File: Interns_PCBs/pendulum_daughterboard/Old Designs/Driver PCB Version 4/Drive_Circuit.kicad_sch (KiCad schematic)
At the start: 13 parts, among them IC1 MAX9928FAUA+, J2 Coil, Q1 BC858W, Q2 BD911

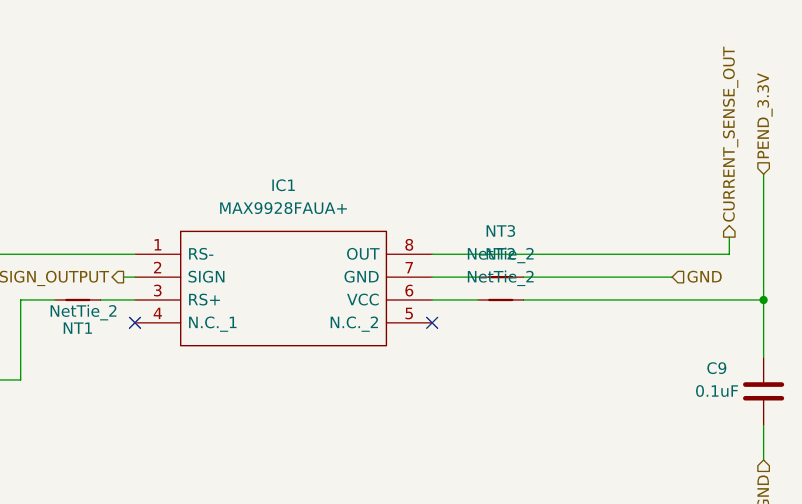
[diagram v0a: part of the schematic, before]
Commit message: Level Shifting Daughterboard
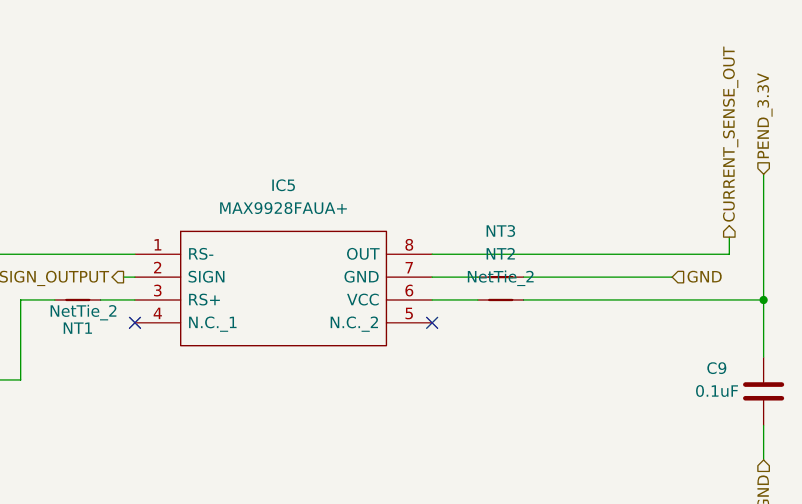
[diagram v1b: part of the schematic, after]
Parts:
- NT3: value NetTie_2 -> (none); footprint NetTie:NetTie-2_SMD_Pad0.5mm -> (none)
- renumbered IC1 to IC5
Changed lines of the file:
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@@
     (in_bom yes) (on_board yes) (fields_autoplaced)
     (property "Reference" "NT3" (id 0) (at 250.19 72.39 0))
-    (property "Value" "NetTie_2" (id 1) (at 250.19 74.93 0))
-    (property "Footprint" "NetTie:NetTie-2_SMD_Pad0.5mm" (id 2) (at 250.19 77.47 0)
+    (property "Value" "" (id 1) (at 250.19 74.93 0))
+    (property "Footprint" "" (id 2) (at 250.19 77.47 0)
       (effects (font (size 1.27 1.27)) hide)
     )
@@
   (symbol (lib_id "MAX9928FAUA+:MAX9928FAUA+") (at 209.55 74.93 0) (unit 1)
     (in_bom yes) (on_board yes) (fields_autoplaced)
-    (property "Reference" "IC1" (id 0) (at 226.06 67.31 0))
+    (property "Reference" "IC5" (id 0) (at 226.06 67.31 0))
     (property "Value" "MAX9928FAUA+" (id 1) (at 226.06 69.85 0))
     (property "Footprint" "Sensor_Current:SOP65P490X110-8N" (id 2) (at 238.76 72.39 0)
